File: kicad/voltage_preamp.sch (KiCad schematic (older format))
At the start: 34 parts, among them J1 Conn_Coaxial, J2 Conn_01x01_Male, J3 Conn_01x01_Male, J4 Conn_01x01_Male, J5 Conn_Coaxial, J6 Conn_01x02_Male, U1 lmp7721, U2 lmp7721, U3 lmp7721, U4 OPA211, U6 OPA211

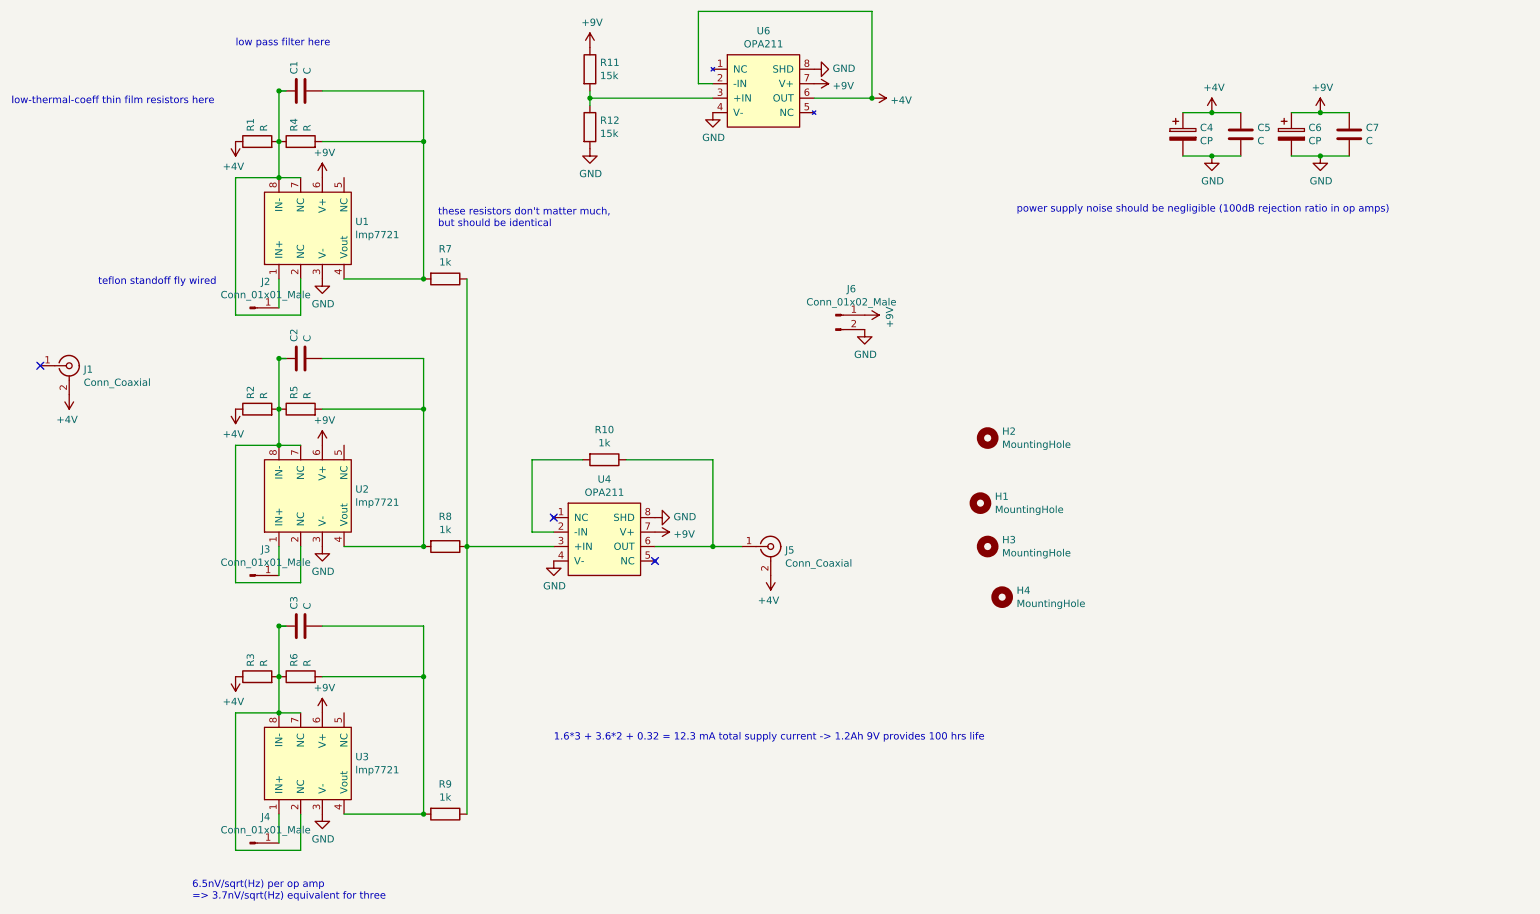
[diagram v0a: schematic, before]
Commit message: fixed bypass cap network
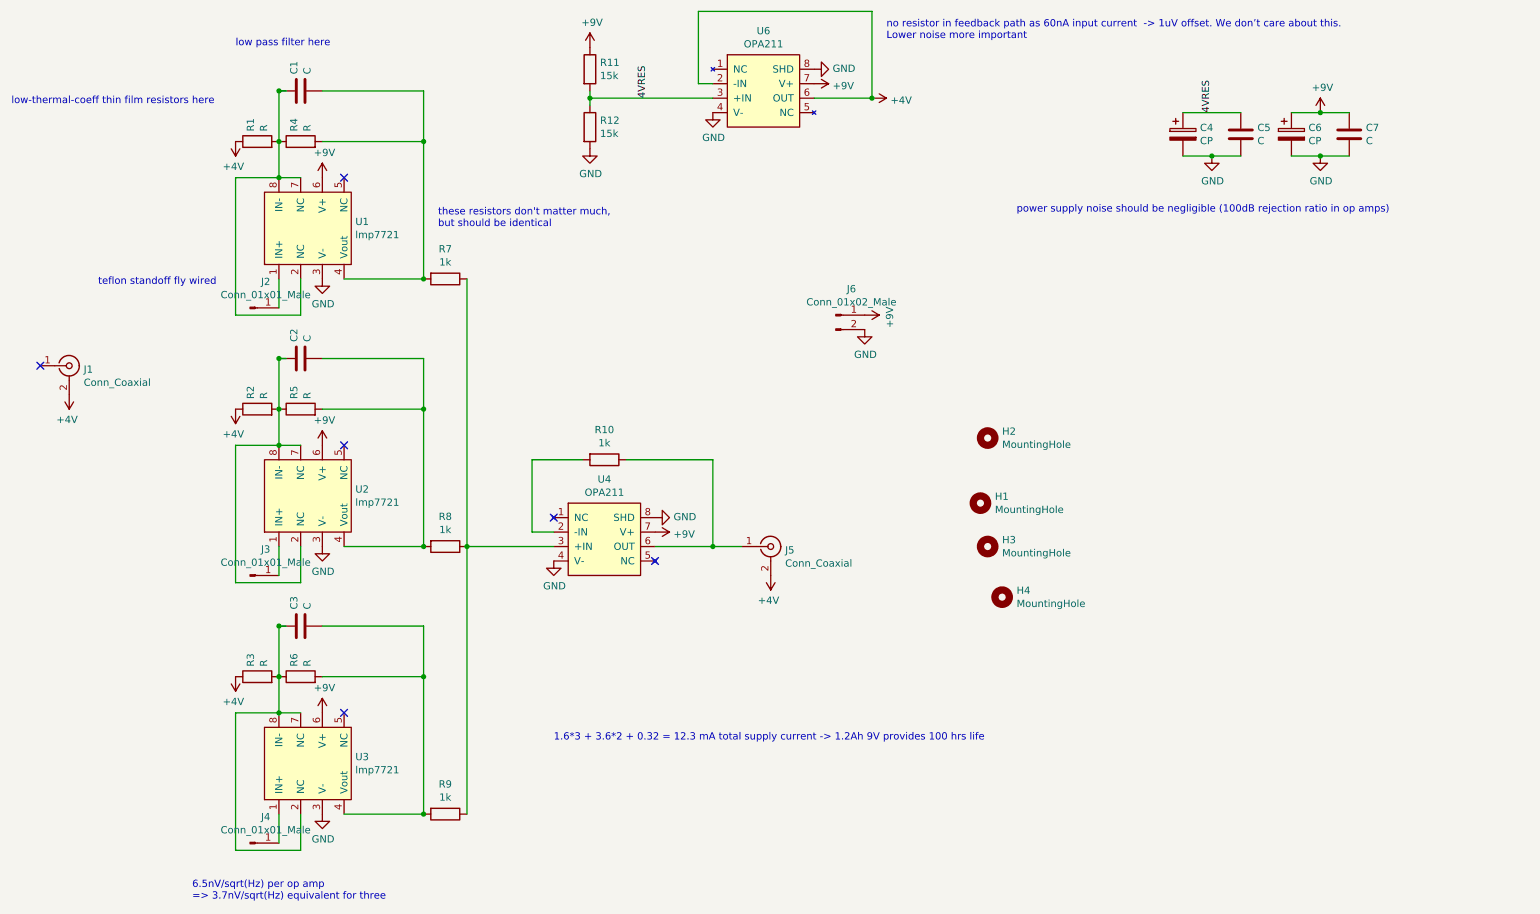
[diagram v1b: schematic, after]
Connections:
- net labels added: 4VRES
- wire segments 68 -> 67
- no-connect marks 3 -> 6
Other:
- note added: "no resistor in feedback path as 60nA input current -> 1uV offset. We don’t care about this. \nLower noise more important"
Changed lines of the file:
@@
-$EndComp
-$Comp
-L power:+4V #PWR0109
-U 1 1 60900970
-P 8950 1250
-F 0 "#PWR0109" H 8950 1100 50  0001 C CNN
-F 1 "+4V" H 8965 1423 50  0000 C CNN
-F 2 "" H 8950 1250 50  0001 C CNN
-F 3 "" H 8950 1250 50  0001 C CNN
-	1    8950 1250
-	1    0    0    -1
 $EndComp
 $Comp
@@
 	1    0    0    -1
 $EndComp
-Wire Wire Line
-	8750 1250 8950 1250
-Connection ~ 8950 1250
-Wire Wire Line
-	8950 1250 9150 1250
 Wire Wire Line
 	8750 1550 8950 1550
@@
 	5400 1050 5400 550
 Wire Wire Line
-	5400 550  6600 550
-Wire Wire Line
 	6600 550  6600 1150
 Wire Wire Line
@@
 Wire Wire Line
 	4650 1150 4650 1200
+Text Label 5050 1150 1    50   ~ 0
+4VRES
+Wire Wire Line
+	8750 1250 9150 1250
+Text Label 8950 1250 1    50   ~ 0
+4VRES
+Text Notes 6700 750  0    50   ~ 0
+no resistor in feedback path as 60nA input current  -> 1uV offset. We don’t care about this. \nLower noise more important
+Wire Wire Line
+	5400 550  6600 550
+NoConn ~ 2950 1700
+NoConn ~ 2950 3550
+NoConn ~ 2950 5400
 $EndSCHEMATC

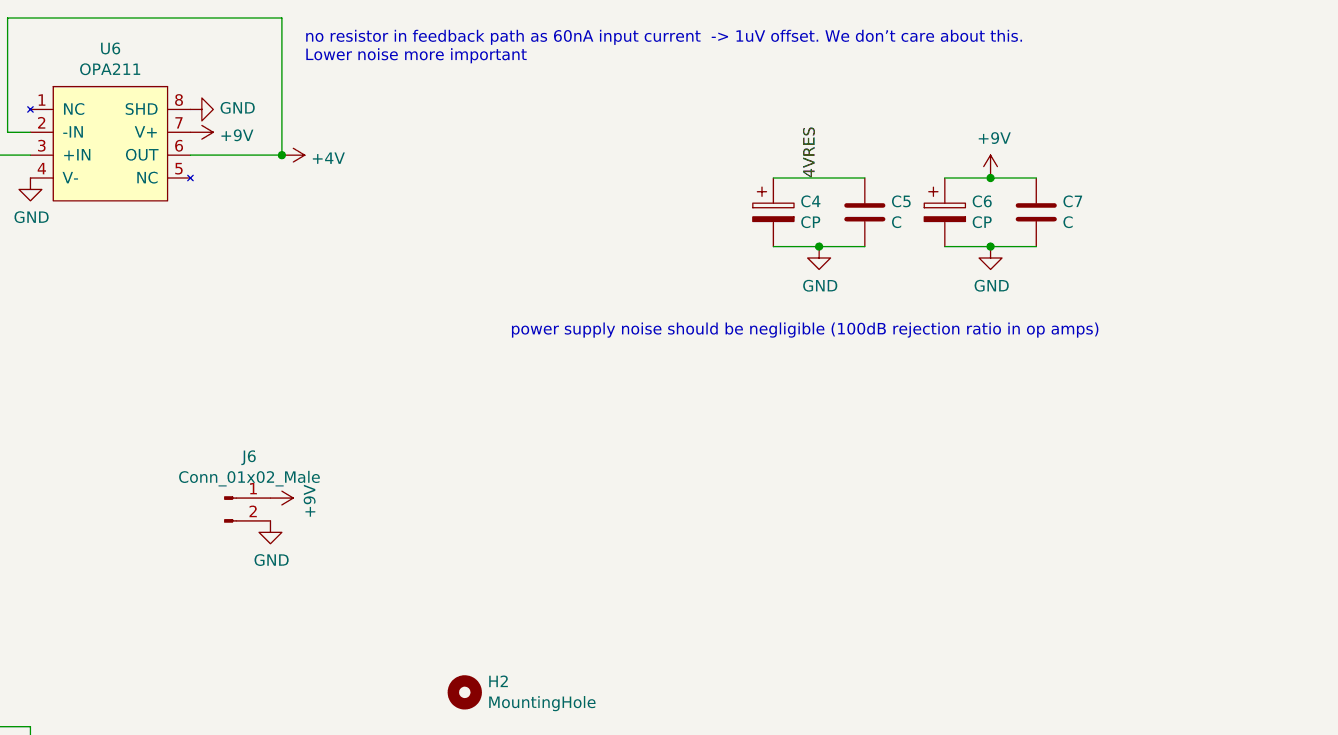
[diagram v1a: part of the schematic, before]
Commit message: now using 4.5V of AAA cells for power, power input available, SMAs for power input and output
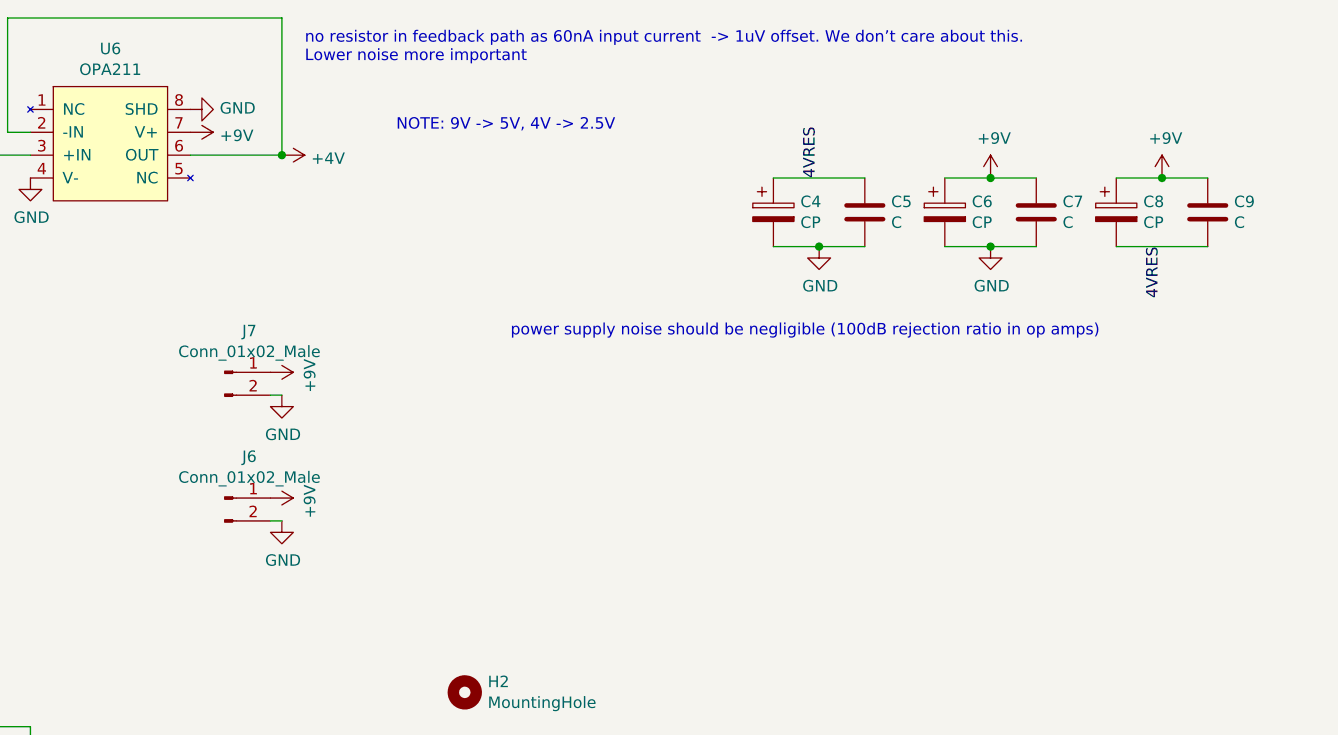
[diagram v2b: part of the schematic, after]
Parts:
- added C8: CP, Connector_PinHeader_2.54mm:PinHeader_1x02_P2.54mm_Vertical, symbol Device:CP
- added C9: C, Capacitor_SMD:C_0805_2012Metric_Pad1.15x1.40mm_HandSolder, symbol Device:C
- added J7: Conn_01x02_Male, Connector_Coaxial:SMA_Molex_73251-2200_Horizontal, symbol Connector:Conn_01x02_Male
- J5: footprint Connector_Coaxial:BNC_Amphenol_B6252HB-NPP3G-50_Horizontal -> Connector_Coaxial:SMA_Molex_73251-2200_Horizontal
- J6: footprint Connector_PinHeader_2.54mm:PinHeader_1x02_P2.54mm_Vertical -> Battery:BatteryHolder_Keystone_2479_3xAAA
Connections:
- wire segments 67 -> 72
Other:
- note added: "NOTE: 9V -> 5V, 4V -> 2.5V"
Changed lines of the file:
@@
 F 0 "J5" H 6000 4225 50  0000 L CNN
 F 1 "Conn_Coaxial" H 6000 4134 50  0000 L CNN
-F 2 "Connector_Coaxial:BNC_Amphenol_B6252HB-NPP3G-50_Horizontal" H 5900 4250 50  0001 C CNN
+F 2 "Connector_Coaxial:SMA_Molex_73251-2200_Horizontal" H 5900 4250 50  0001 C CNN
 F 3 " ~" H 5900 4250 50  0001 C CNN
 	1    5900 4250
@@
 F 0 "J6" H 6458 2831 50  0000 C CNN
 F 1 "Conn_01x02_Male" H 6458 2740 50  0000 C CNN
-F 2 "Connector_PinHeader_2.54mm:PinHeader_1x02_P2.54mm_Vertical" H 6350 2650 50  0001 C CNN
+F 2 "Battery:BatteryHolder_Keystone_2479_3xAAA" H 6350 2650 50  0001 C CNN
 F 3 "~" H 6350 2650 50  0001 C CNN
 	1    6350 2650
@@
 $EndComp
 $Comp
-L power:GND #PWR0122
-U 1 1 609A2210
-P 6550 2750
-F 0 "#PWR0122" H 6550 2500 50  0001 C CNN
-F 1 "GND" H 6555 2577 50  0000 C CNN
-F 2 "" H 6550 2750 50  0001 C CNN
-F 3 "" H 6550 2750 50  0001 C CNN
-	1    6550 2750
-	1    0    0    -1
-$EndComp
-$Comp
 L Mechanical:MountingHole H2
 U 1 1 609D69A9
@@
 NoConn ~ 2950 3550
 NoConn ~ 2950 5400
+$Comp
+L Connector:Conn_01x02_Male J7
+U 1 1 609618E4
+P 6350 2100
+F 0 "J7" H 6458 2281 50  0000 C CNN
+F 1 "Conn_01x02_Male" H 6458 2190 50  0000 C CNN
+F 2 "Connector_Coaxial:SMA_Molex_73251-2200_Horizontal" H 6350 2100 50  0001 C CNN
+F 3 "~" H 6350 2100 50  0001 C CNN
+	1    6350 2100
+	1    0    0    -1
+$EndComp
+$Comp
+L power:+9V #PWR0109
+U 1 1 609650C0
+P 6550 2100
+F 0 "#PWR0109" H 6550 1950 50  0001 C CNN
+F 1 "+9V" H 6565 2273 50  0000 C CNN
+F 2 "" H 6550 2100 50  0001 C CNN
+F 3 "" H 6550 2100 50  0001 C CNN
+	1    6550 2100
+	0    1    1    0
+$EndComp
+$Comp
+L power:GND #PWR0122
+U 1 1 609A2210
+P 6600 2750
+F 0 "#PWR0122" H 6600 2500 50  0001 C CNN
+F 1 "GND" H 6605 2577 50  0000 C CNN
+F 2 "" H 6600 2750 50  0001 C CNN
+F 3 "" H 6600 2750 50  0001 C CNN
+	1    6600 2750
+	1    0    0    -1
+$EndComp
+$Comp
+L power:GND #PWR0127
+U 1 1 60967363
+P 6600 2200
+F 0 "#PWR0127" H 6600 1950 50  0001 C CNN
+F 1 "GND" H 6605 2027 50  0000 C CNN
+F 2 "" H 6600 2200 50  0001 C CNN
+F 3 "" H 6600 2200 50  0001 C CNN
+	1    6600 2200
+	1    0    0    -1
+$EndComp
+Wire Wire Line
+	6550 2200 6600 2200
+Wire Wire Line
+	6550 2750 6600 2750
+$Comp
+L power:+9V #PWR0128
+U 1 1 609AB965
+P 10450 1250
+F 0 "#PWR0128" H 10450 1100 50  0001 C CNN
+F 1 "+9V" H 10465 1423 50  0000 C CNN
+F 2 "" H 10450 1250 50  0001 C CNN
+F 3 "" H 10450 1250 50  0001 C CNN
+	1    10450 1250
+	1    0    0    -1
+$EndComp
+$Comp
+L Device:C C9
+U 1 1 609AB971
+P 10650 1400
+F 0 "C9" H 10765 1446 50  0000 L CNN
+F 1 "C" H 10765 1355 50  0000 L CNN
+F 2 "Capacitor_SMD:C_0805_2012Metric_Pad1.15x1.40mm_HandSolder" H 10688 1250 50  0001 C CNN
+F 3 "~" H 10650 1400 50  0001 C CNN
+	1    10650 1400
+	1    0    0    -1
+$EndComp
+$Comp
+L Device:CP C8
+U 1 1 609AB977
+P 10250 1400
+F 0 "C8" H 10368 1446 50  0000 L CNN
+F 1 "CP" H 10368 1355 50  0000 L CNN
+F 2 "Connector_PinHeader_2.54mm:PinHeader_1x02_P2.54mm_Vertical" H 10288 1250 50  0001 C CNN
+F 3 "~" H 10250 1400 50  0001 C CNN
+	1    10250 1400
+	1    0    0    -1
+$EndComp
+Wire Wire Line
+	10250 1250 10450 1250
+Connection ~ 10450 1250
+Wire Wire Line
+	10450 1250 10650 1250
+Text Label 10450 1550 3    50   ~ 0
+4VRES
+Wire Wire Line
+	10250 1550 10650 1550
+Text Notes 7100 1050 0    50   ~ 0
+NOTE: 9V -> 5V, 4V -> 2.5V
 $EndSCHEMATC

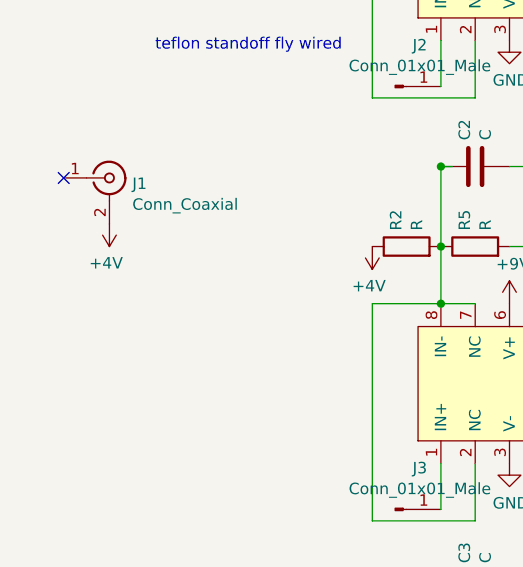
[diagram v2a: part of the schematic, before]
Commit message: fixed via shielding, now using bnc as output and power connectors
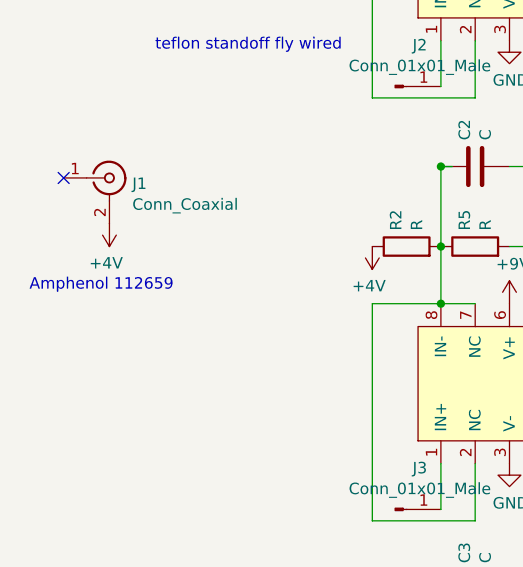
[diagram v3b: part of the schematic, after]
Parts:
- J5, J7: footprint Connector_Coaxial:SMA_Molex_73251-2200_Horizontal -> Connector_Coaxial:BNC_Amphenol_B6252HB-NPP3G-50_Horizontal
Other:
- note added: "Amphenol 112659"
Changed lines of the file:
@@
 F 0 "J5" H 6000 4225 50  0000 L CNN
 F 1 "Conn_Coaxial" H 6000 4134 50  0000 L CNN
-F 2 "Connector_Coaxial:SMA_Molex_73251-2200_Horizontal" H 5900 4250 50  0001 C CNN
+F 2 "Connector_Coaxial:BNC_Amphenol_B6252HB-NPP3G-50_Horizontal" H 5900 4250 50  0001 C CNN
 F 3 " ~" H 5900 4250 50  0001 C CNN
 	1    5900 4250
@@
 F 0 "J7" H 6458 2281 50  0000 C CNN
 F 1 "Conn_01x02_Male" H 6458 2190 50  0000 C CNN
-F 2 "Connector_Coaxial:SMA_Molex_73251-2200_Horizontal" H 6350 2100 50  0001 C CNN
+F 2 "Connector_Coaxial:BNC_Amphenol_B6252HB-NPP3G-50_Horizontal" H 6350 2100 50  0001 C CNN
 F 3 "~" H 6350 2100 50  0001 C CNN
 	1    6350 2100
@@
 Text Notes 7100 1050 0    50   ~ 0
 NOTE: 9V -> 5V, 4V -> 2.5V
+Text Notes 700  3500 0    50   ~ 0
+Amphenol 112659
 $EndSCHEMATC
